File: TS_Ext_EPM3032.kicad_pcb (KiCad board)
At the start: 2 copper layers, 99.1 x 78.1 mm, 56 parts, among them J1 JTAG, J2 CD_IN, J3 System Ext, J4 AUDIO OUT, J5 AudioJack3_SwitchTR, Q1 BC547, Q2 BC547, Q3 BC547, U1 EPM3064ALC44, U2 AMS1117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

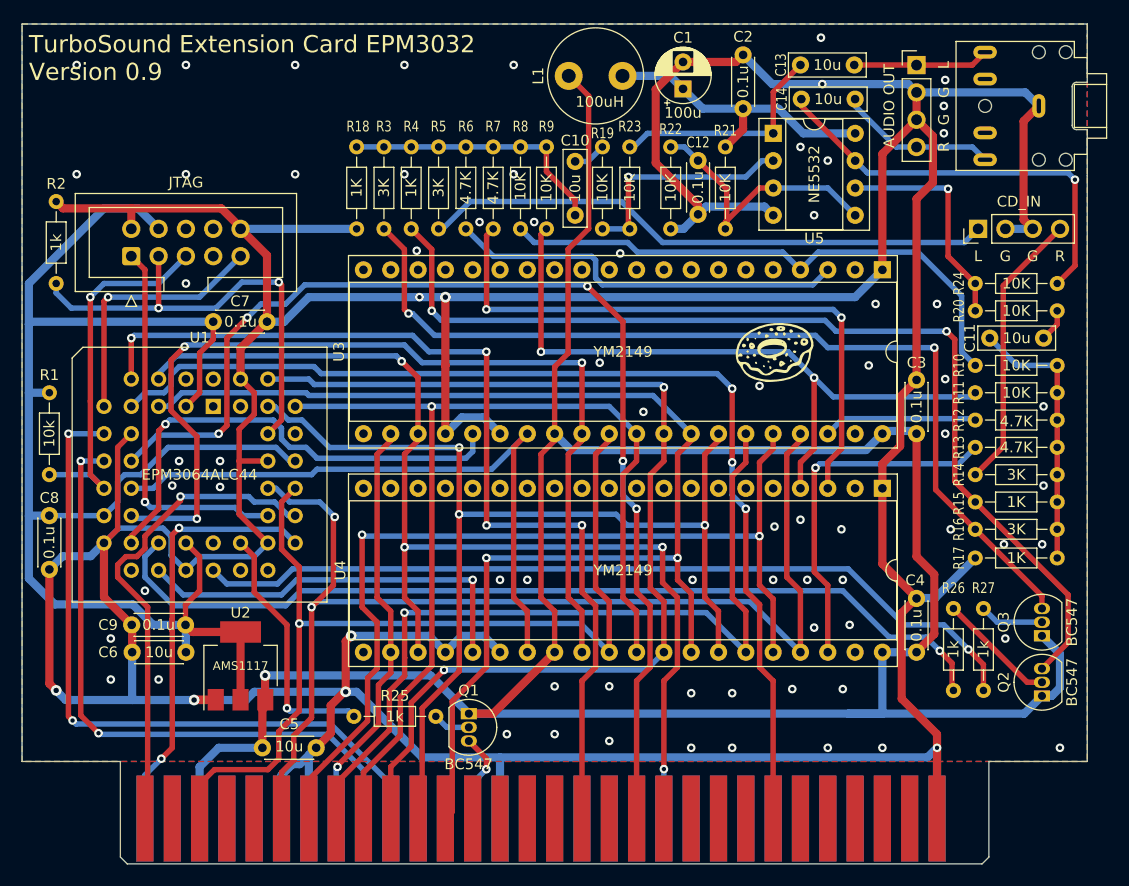
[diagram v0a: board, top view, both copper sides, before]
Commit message: * Bump to version 1.0 * BOM, schematics and gerbers added
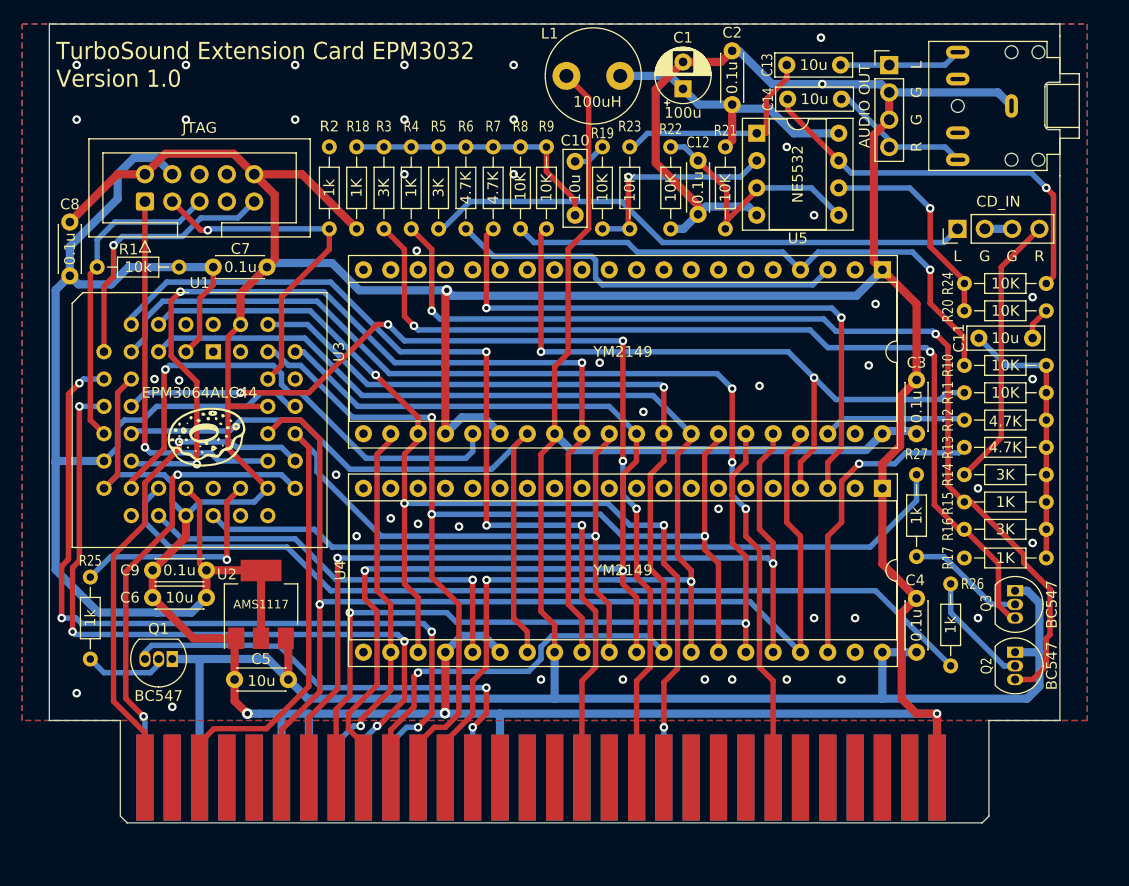
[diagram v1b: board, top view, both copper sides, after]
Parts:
- moved LOGO1 53.4 mm to (42.5, 64.1)
- moved Q1 28.0 mm to (39.4, 84.5), turned to 180 degrees
- moved R25 27.7 mm to (31.8, 76.8), turned to -90 degrees
- moved R2 25.9 mm to (54.0, 36.8)
- moved C8 22.4 mm to (29.8, 48.8), turned to 90 degrees
- moved R27 21.0 mm to (108.6, 67.3), turned to -90 degrees
- moved R1 19.8 mm to (32.4, 48.0), turned to 0 degrees
- moved C5 6.79 mm to (50.2, 86.4), turned to 180 degrees
- moved U2 6.02 mm to (47.6, 79.4)
- moved C9 5.44 mm to (42.5, 76.2)
- moved C6 5.43 mm to (42.5, 78.7)
- moved J1 5.24 mm to (36.8, 41.9)
- moved C7 5.08 mm to (43.2, 48.0)
- moved U1 5.08 mm to (43.2, 55.9)
- moved Q3 4.88 mm to (117.8, 78.1), turned to -90 degrees
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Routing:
- net GND: track 527.2 -> 437.4 mm, vias 77 -> 49
- net /~{IORQGE}: track 5.10 -> 43.2 mm, vias 1 -> 2
- net +5V: track 236.0 -> 215.5 mm, vias 1 -> 0
- net /~{WR}: track 106.5 -> 91.7 mm
- net /TDO: track 42.7 -> 32.1 mm, vias 2 -> 1
- net /A1: track 62.2 -> 72.5 mm, vias 2 -> 4
- net /TAPEOUT33: track 78.8 -> 70.8 mm, vias 1 -> 0
- net +3.3V: track 139.5 -> 132.1 mm
- net /CLK350: track 38.9 -> 32.1 mm
- net /A0: track 58.7 -> 65.5 mm, vias 2 -> 4
- net /D4: track 116.6 -> 110.8 mm
- net Net-(Q3-Pad2): track 5.97 -> 11.0 mm
- net /TMS: track 34.4 -> 29.8 mm, vias 1 -> 0
- net /D1: track 88.0 -> 83.6 mm
- net /YM_1_C: track 33.4 -> 29.1 mm
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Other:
- board size 99.1 x 78.1 mm -> 94 x 74.3 mm

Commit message: Remove transistors, reorganize folders
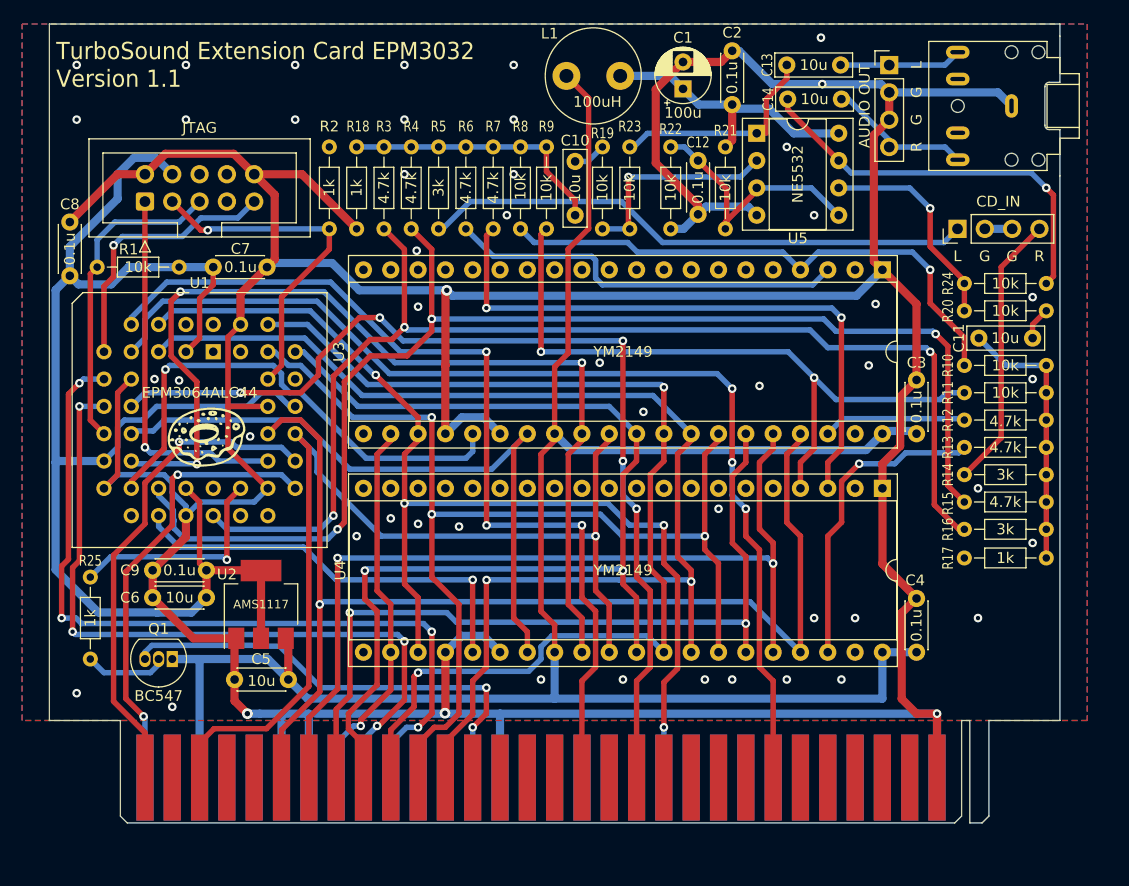
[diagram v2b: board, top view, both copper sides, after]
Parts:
- removed Q2, Q3: BC547, Package_TO_SOT_THT:TO-92_Inline
- removed R26, R27: 1k, Resistor_THT:R_Axial_DIN0204_L3.6mm_D1.6mm_P7.62mm_Horizontal
- R10, R11, R19, R20, R21, R22, R23, R24, R8, R9: value 10K -> 10k
- R12, R13, R6, R7: value 4.7K -> 4.7k
- R14, R16, R5: value 3K -> 3k
- R15, R4: value 1K -> 4.7k
- R17, R18: value 1K -> 1k
- R3: value 3K -> 4.7k
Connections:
- U1 pad 21: /BEEPER33 -> /BEEPER
- U1 pad 24: /TAPEOUT33 -> /TAPEOUT
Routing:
- net /BEEPER33: track 84.2 -> 0.00 mm
- net /TAPEOUT33: track 70.8 -> 0.00 mm
- net +5V: track 215.5 -> 187.7 mm
- net /TAPEOUT: track 87.4 -> 111.6 mm, vias 2 -> 3
- net /BEEPER: track 95.4 -> 118.9 mm, vias 2 -> 3
- net Net-(Q3-Pad2): track 11.0 -> 0.00 mm
- net Net-(Q2-Pad2): track 10.7 -> 0.00 mm
- net /~{WR}: track 91.7 -> 93.1 mm
- net /A8_1: track 38.4 -> 39.0 mm
- net GND: vias 49 -> 51
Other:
- outline, holes or cut-outs redrawn

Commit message: Fix YM2149F symbol
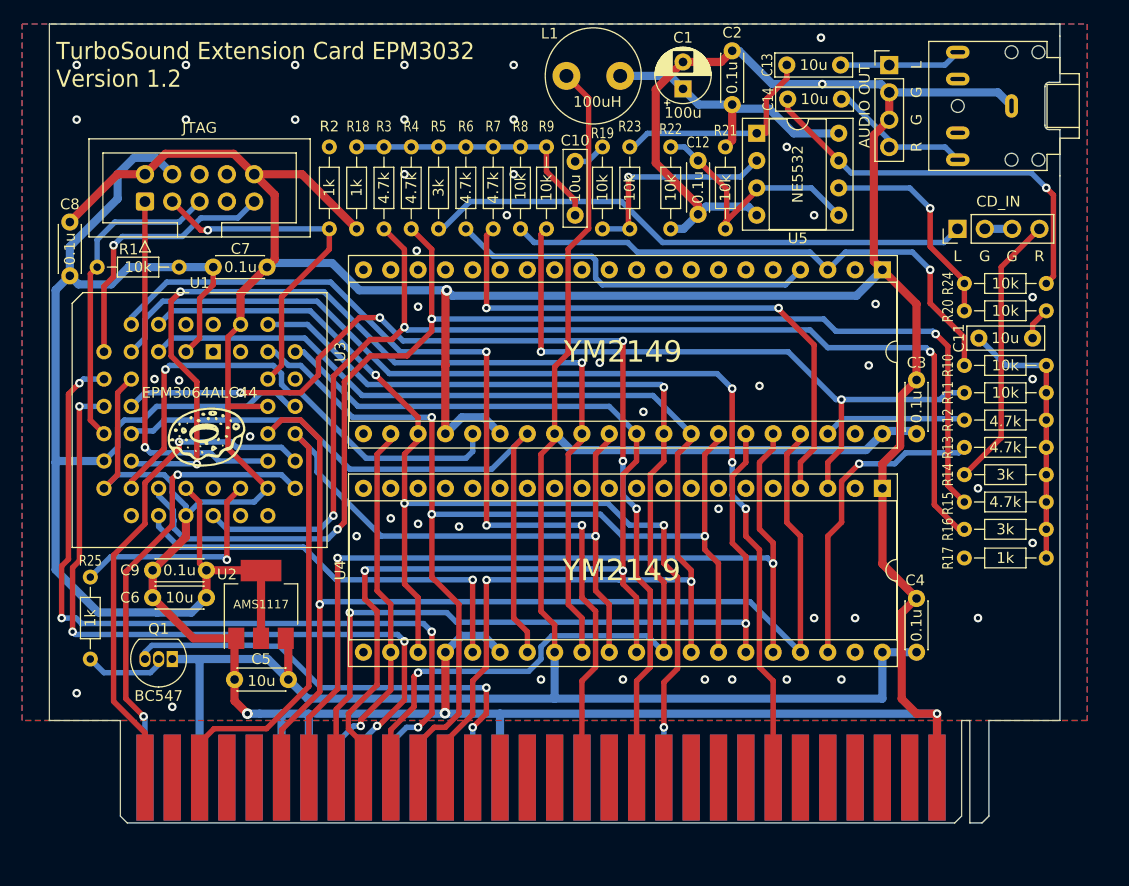
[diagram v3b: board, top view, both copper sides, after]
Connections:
- U3 pad 3: /YM_0_A -> /YM_0_B
- U3 pad 4: /YM_0_B -> /YM_0_A
- U4 pad 3: /YM_1_A -> /YM_1_B
- U4 pad 4: /YM_1_B -> /YM_1_A
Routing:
- net /YM_1_A: track 57.4 -> 53.5 mm
- net /YM_0_A: track 37.4 -> 34.8 mm
- net /YM_1_B: track 63.9 -> 61.9 mm

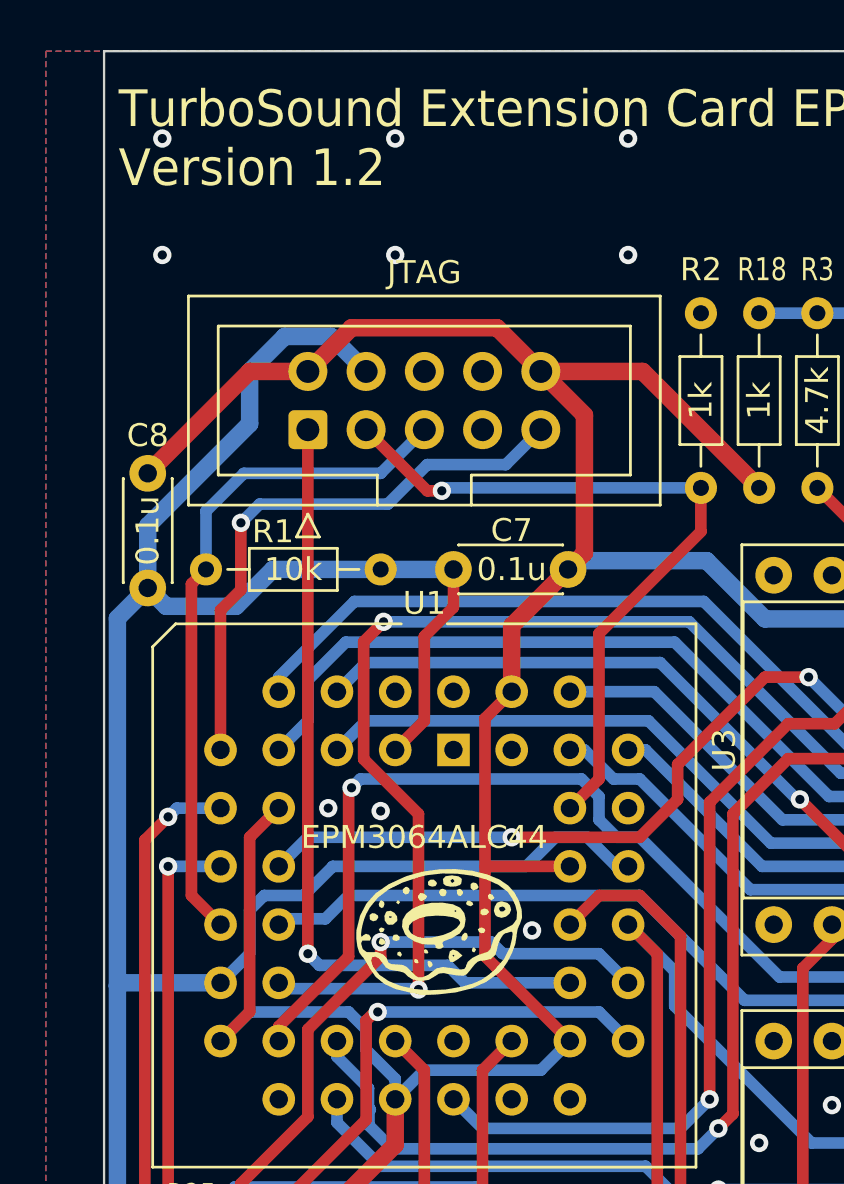
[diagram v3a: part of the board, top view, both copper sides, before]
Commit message: Fix pull-up on JTAG connector
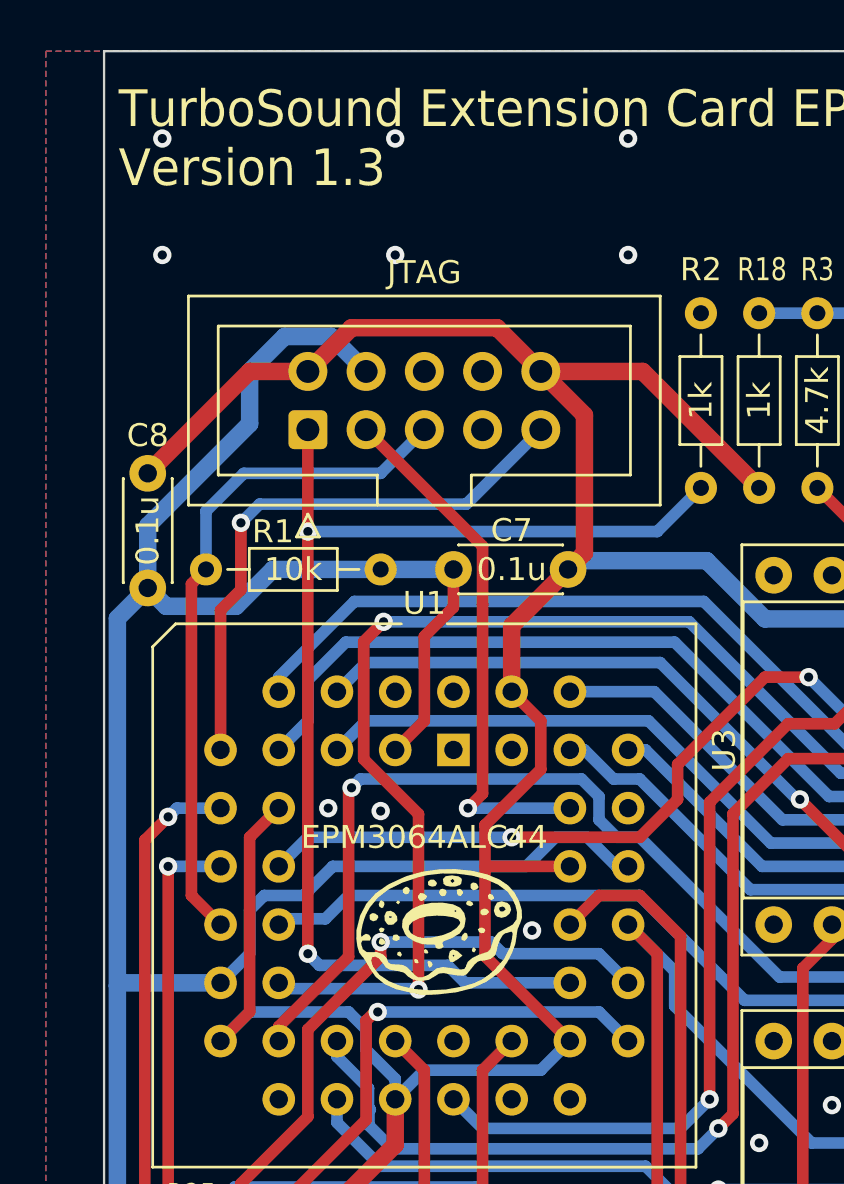
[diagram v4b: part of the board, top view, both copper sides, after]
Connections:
- R2 pad 2: /TDO -> /TCK
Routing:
- net /TCK: track 34.8 -> 52.8 mm, vias 1 -> 2
- net /TDO: track 32.1 -> 23.3 mm
- net GND: track 437.4 -> 438.5 mm

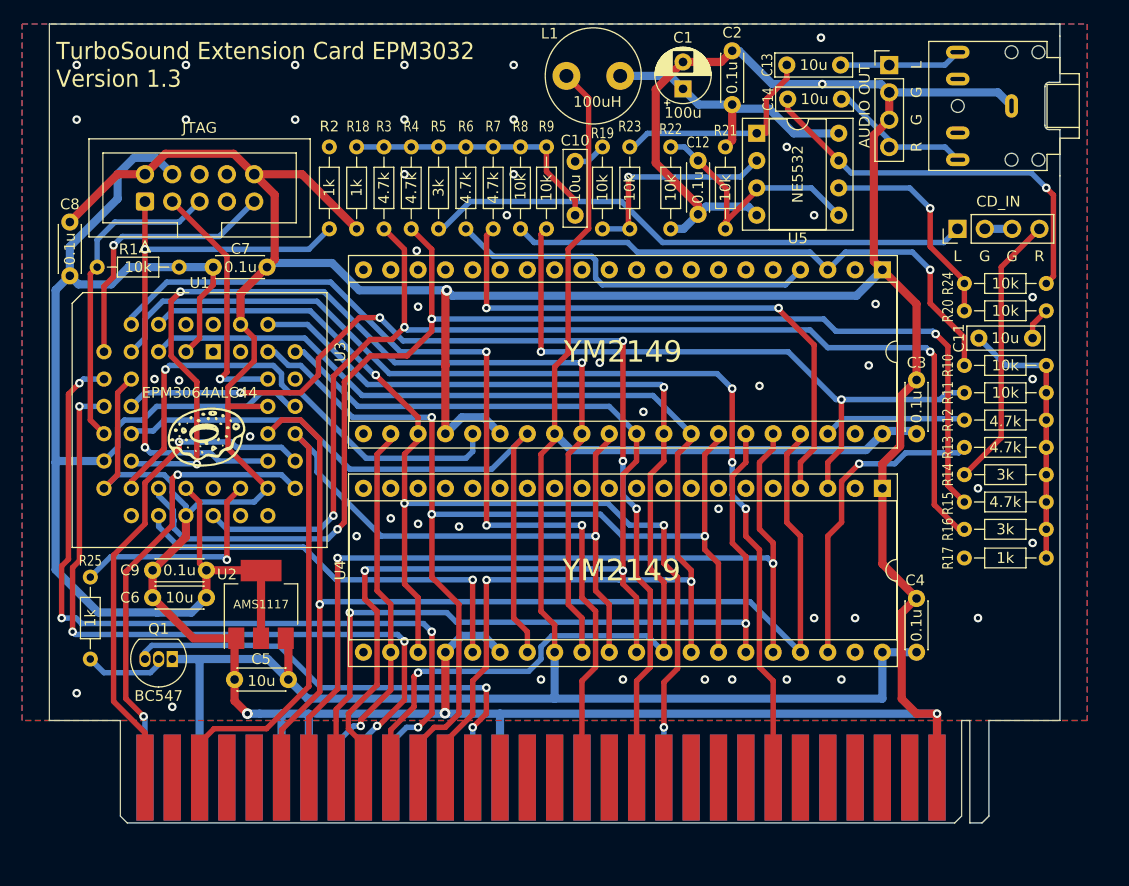
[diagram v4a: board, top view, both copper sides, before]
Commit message: Migrated to KiCad 8, CPLD value fix
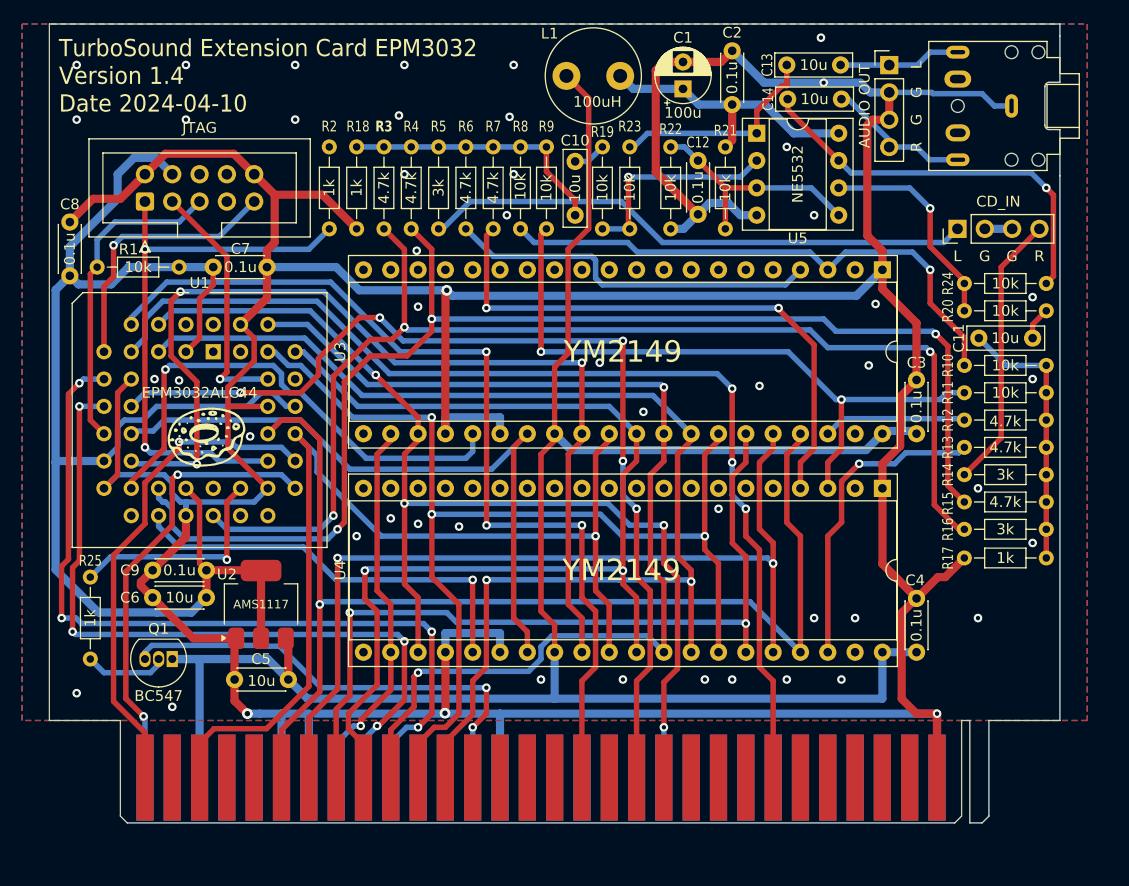
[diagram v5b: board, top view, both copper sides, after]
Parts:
- J5: value AudioJack3_SwitchTR -> SJ1-3525N
- U1: value EPM3064ALC44 -> EPM3032ALC44
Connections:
- J3 pad b15: /~{RDR} -> unconnected-(J3-Pin_b15-Padb15)
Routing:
- net GND: track 438.5 -> 449.0 mm
- net +3.3V: track 132.1 -> 134.0 mm
- net Net-(U5A-+): track 23.8 -> 22.1 mm
- net Net-(C13-Pad1): track 19.1 -> 19.7 mm
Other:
- board text added: "${TITLE} Version ${REVISION} Date ${ISSUE_DATE}"
- board text removed: "${TITLE} Version ${REVISION}"
